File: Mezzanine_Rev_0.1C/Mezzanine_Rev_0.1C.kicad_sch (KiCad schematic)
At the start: 63 parts, among them J1 QBUS_DWK_64Pin_MBT, J2 DIP20 Header, J3 DIP20 Header, J4 IDC-64M, J5 IDC-16M, J6 IDC-20M, J7 Conn_01x03_Pin, J8 PLD-16R, U1 1533LI1, U10 74LS07, U11 74LS74, U2 1533TM2, U3 1533LA8, U4 CD4067B, U4.2 CD74HCT4067M, U5 1533LE4, U6 1533AP6, U7 1533AP6, U8 74LS07, U9 74LS07

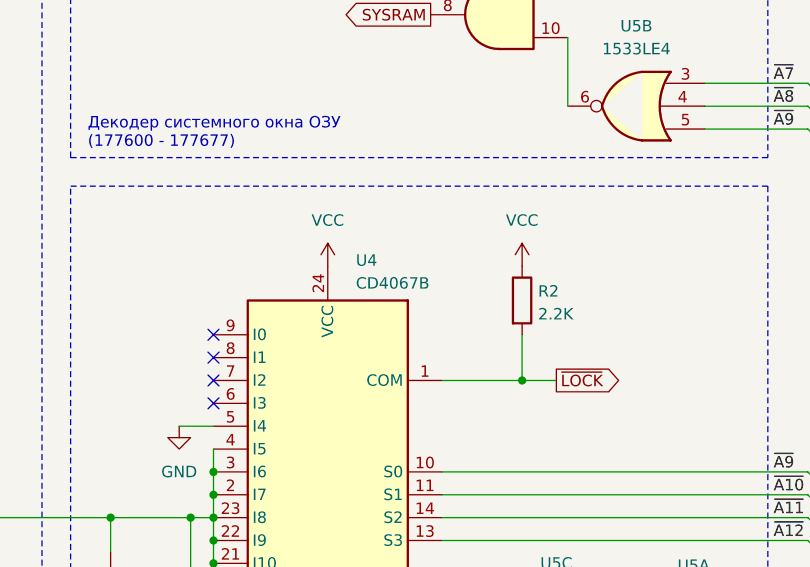
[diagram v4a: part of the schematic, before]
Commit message: Mezzanine: Proper types for U4
Distinguish DIP vs SOIC
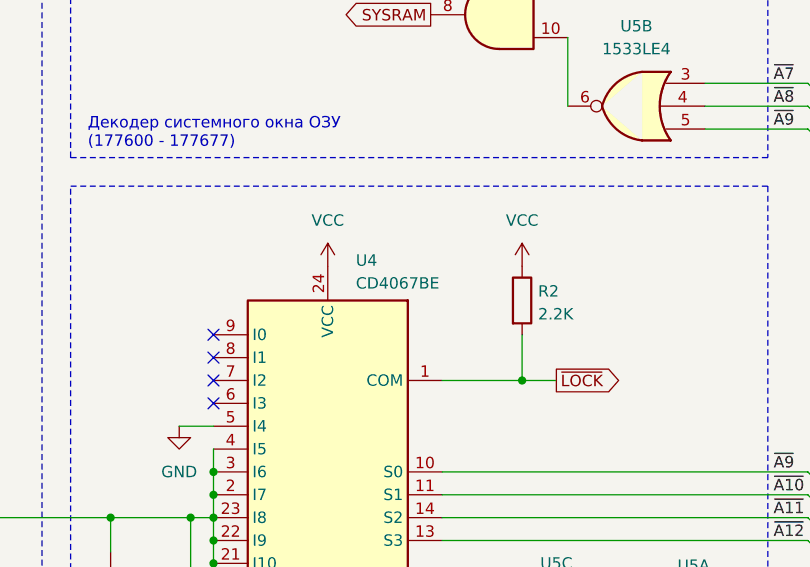
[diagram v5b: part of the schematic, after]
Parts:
- U4: value CD4067B -> CD4067BE
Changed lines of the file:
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@@
 			)
 		)
-		(property "Value" "CD4067B"
+		(property "Value" "CD4067BE"
 			(at 171.3931 77.47 0)
 			(show_name no)

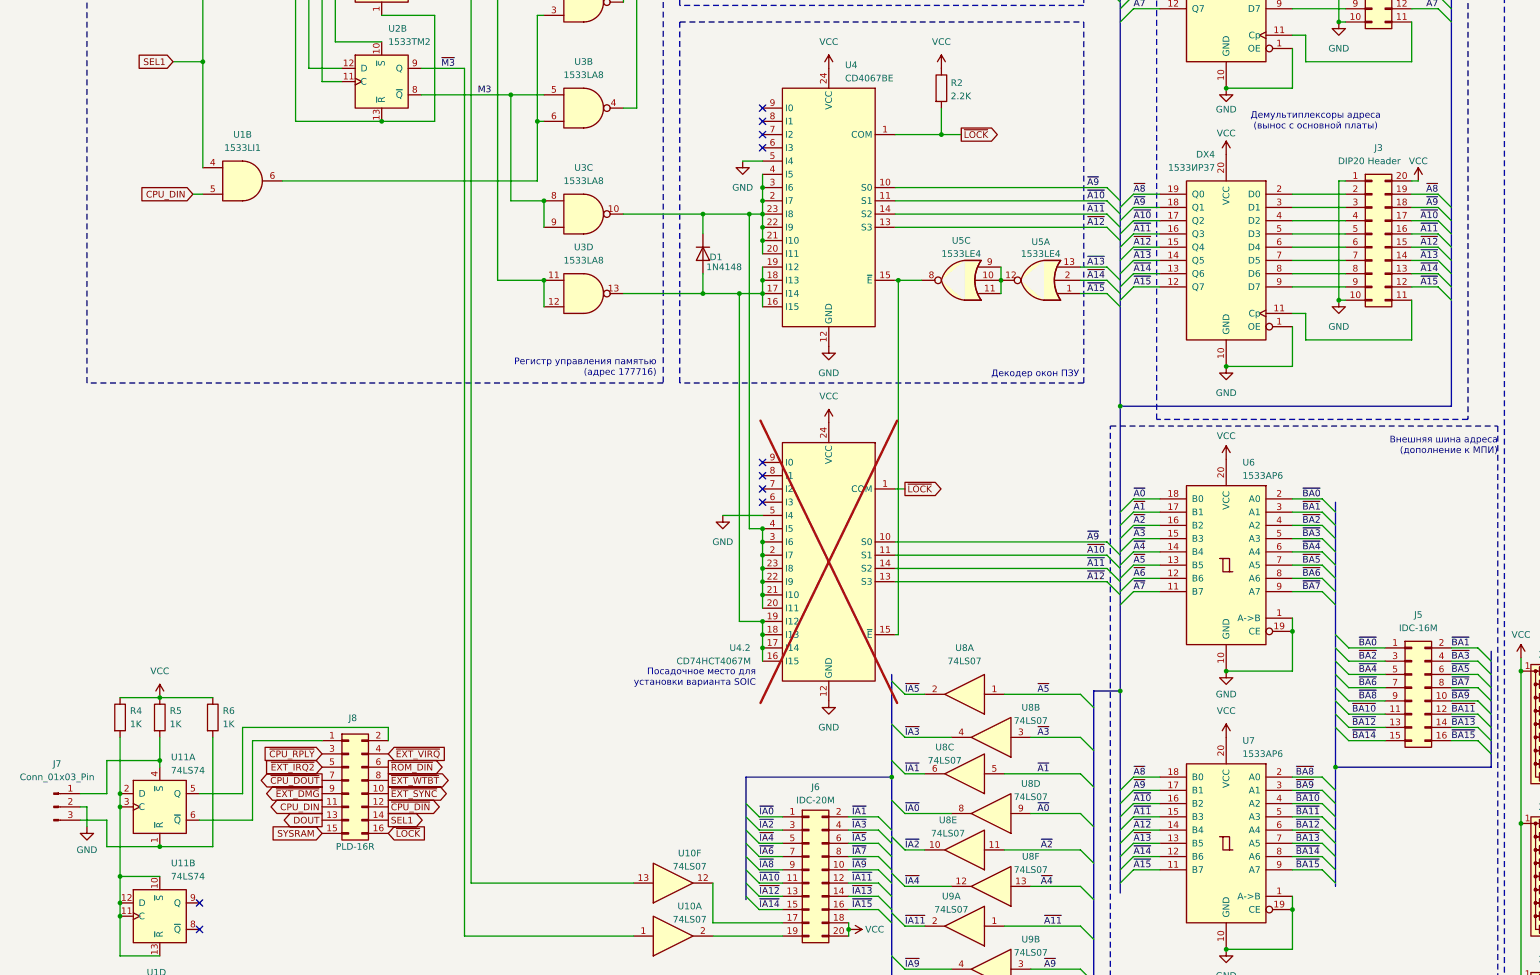
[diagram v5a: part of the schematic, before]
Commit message: Mezzanine: PDF out
PDF version of the mezzanine board schematic.
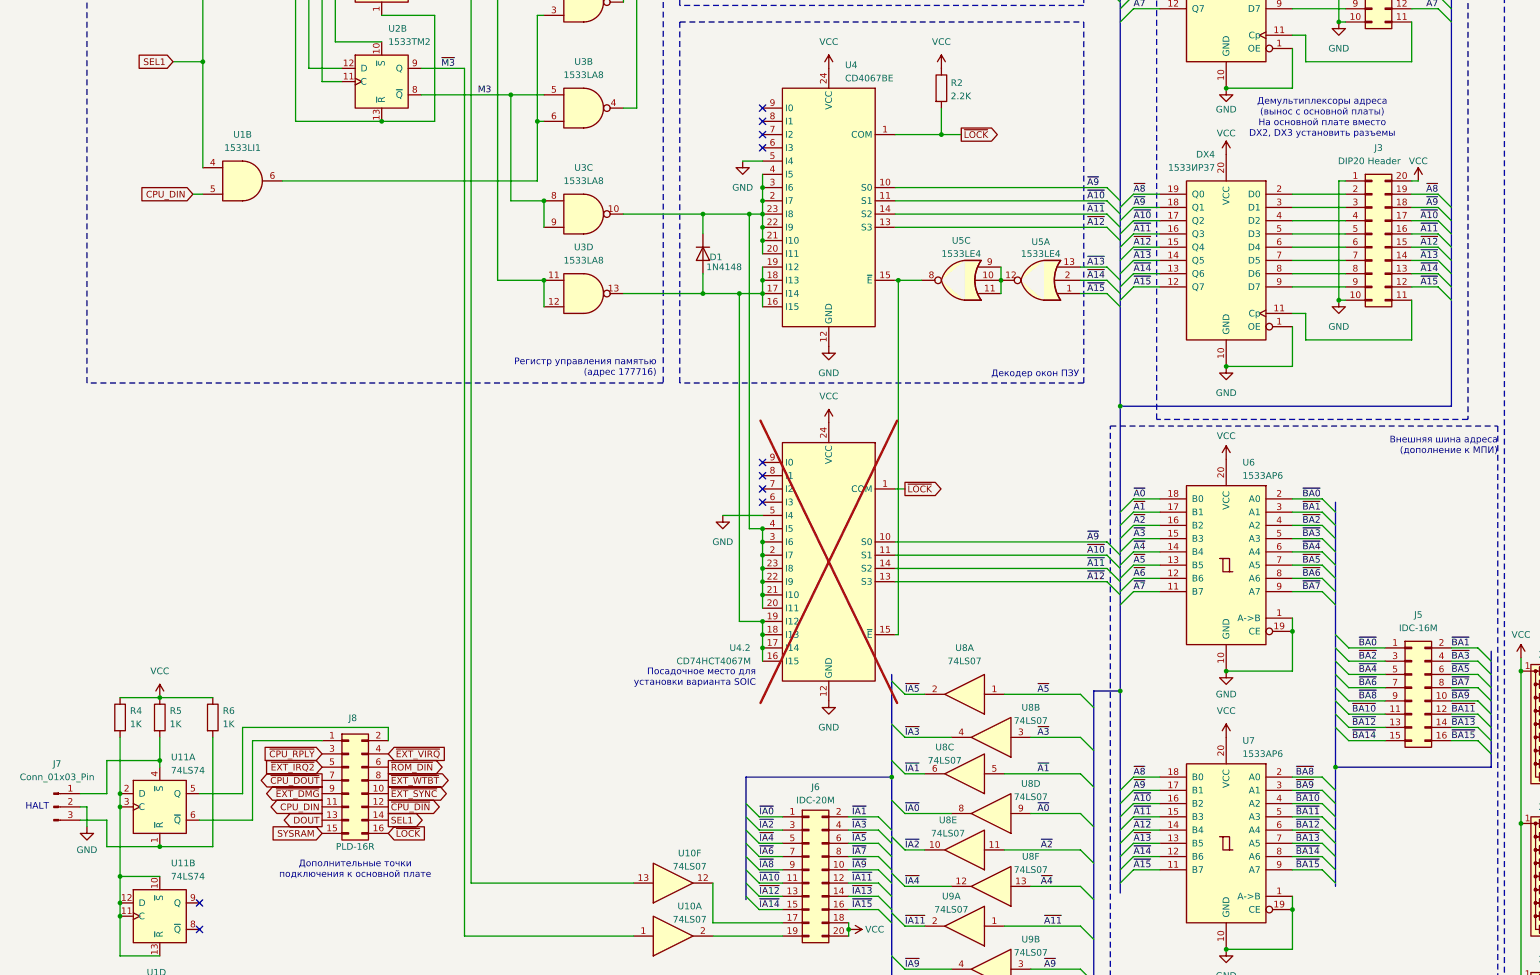
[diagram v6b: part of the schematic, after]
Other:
- note added: "HALT"
- note added: "Демультиплексоры адреса (вынос с основной платы) На основной плате вместо DX2, DX3 установить разъемы"
- note added: "Дополнительные точки подключения к основной плате"
- note removed: "Демультиплексоры адреса (вынос с основной платы)"
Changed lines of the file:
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@@
+		)
+	)
+	(text "HALT "
+		(exclude_from_sim no)
+		(at 16.51 217.17 0)
+		(effects
+			(font
+				(size 1.27 1.27)
+			)
 		)
 	)
@@
 		(exclude_from_sim no)
 		(at 493.395 319.405 0)
+		(effects
+			(font
+				(size 1.27 1.27)
+			)
+		)
+	)
+	(text "Дополнительные точки\nподключения к основной плате"
+		(exclude_from_sim no)
+		(at 77.47 229.235 0)
 		(effects
 			(font
@@
 		)
 	)
-	(text "Демультиплексоры адреса\n(вынос с основной платы)"
+	(text "Демультиплексоры адреса\n(вынос с основной платы)\nНа основной плате вместо\nDX2, DX3 установить разъемы"
 		(exclude_from_sim no)
-		(at 261.62 85.725 0)
+		(at 262.89 85.09 0)
 		(effects
 			(font
